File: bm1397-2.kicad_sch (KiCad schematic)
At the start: 58 parts, among them IC3 BM1397_mode0, IC4 BM1397_mode0, U5 MCP1824T-1802E, U6 MCP1824T-0802E

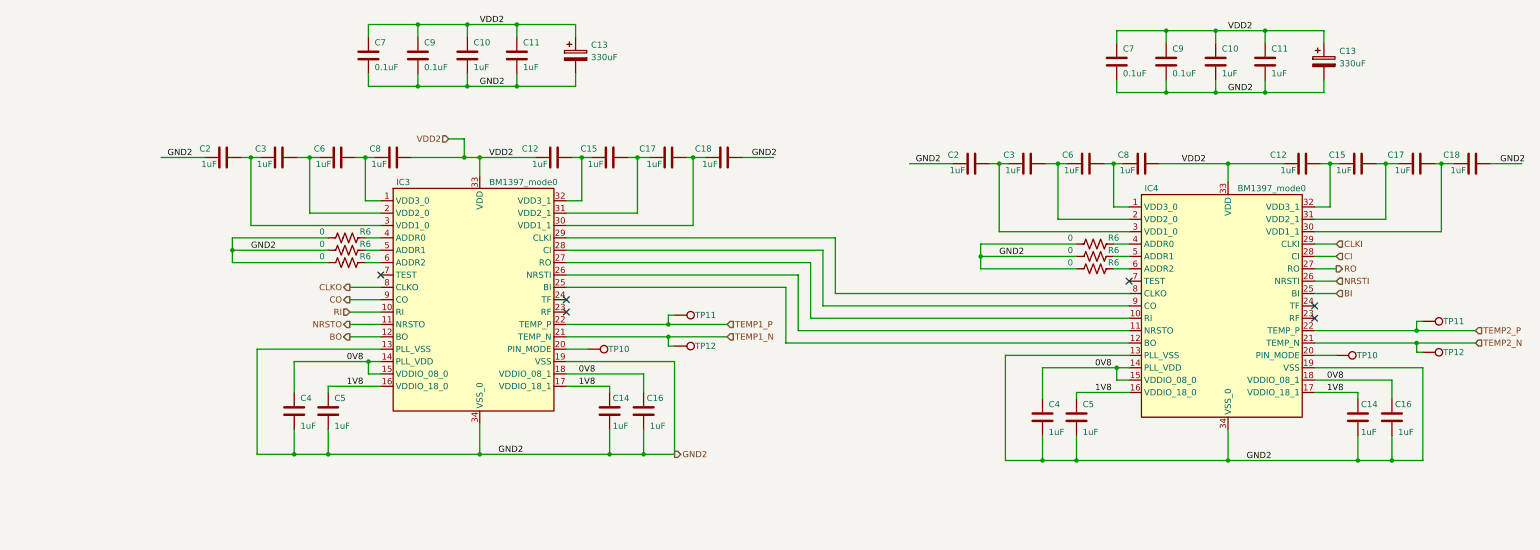
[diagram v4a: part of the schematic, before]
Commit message: some more placements, added level shifters..
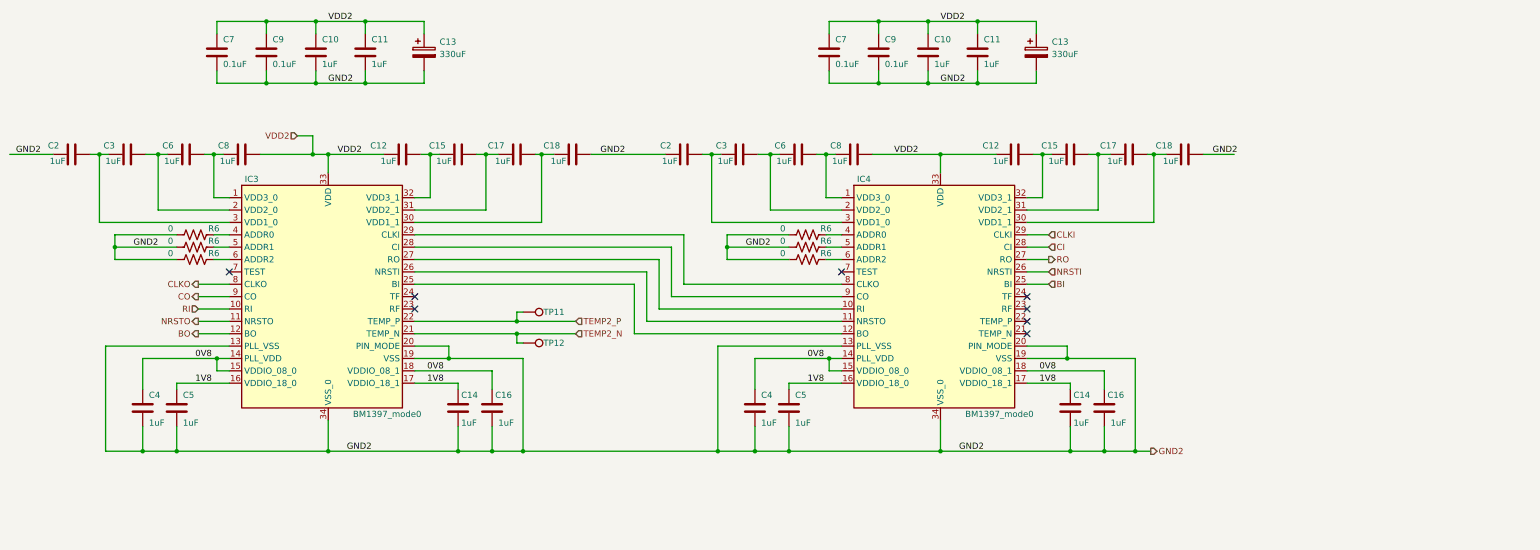
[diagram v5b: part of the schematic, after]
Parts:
- removed TP10 (x2), TP11, TP12: TestPoint, TestPoint:TestPoint_Pad_D1.5mm, symbol Connector:TestPoint
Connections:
- net TEMP1_N is gone; now on net TEMP2_N: IC3.21 (TEMP_N)
- net TEMP1_P is gone; now on net TEMP2_P: IC3.22 (TEMP_P)
- net GND2: now also IC3.20 (PIN_MODE), IC4.20 (PIN_MODE)
- net TEMP2_N: no longer IC4.21 (TEMP_N)
- net TEMP2_P: no longer IC4.22 (TEMP_P)
- no-connect marks 6 -> 8
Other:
- moved on the sheet: C10, C11, C12, C13, C14, C15, C16, C17, C18, C2, C3, C4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
